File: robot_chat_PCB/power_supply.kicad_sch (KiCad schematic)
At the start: 23 parts, among them U2 MP1475DJ-LF-P, U3 MIC5317-3.3xM5

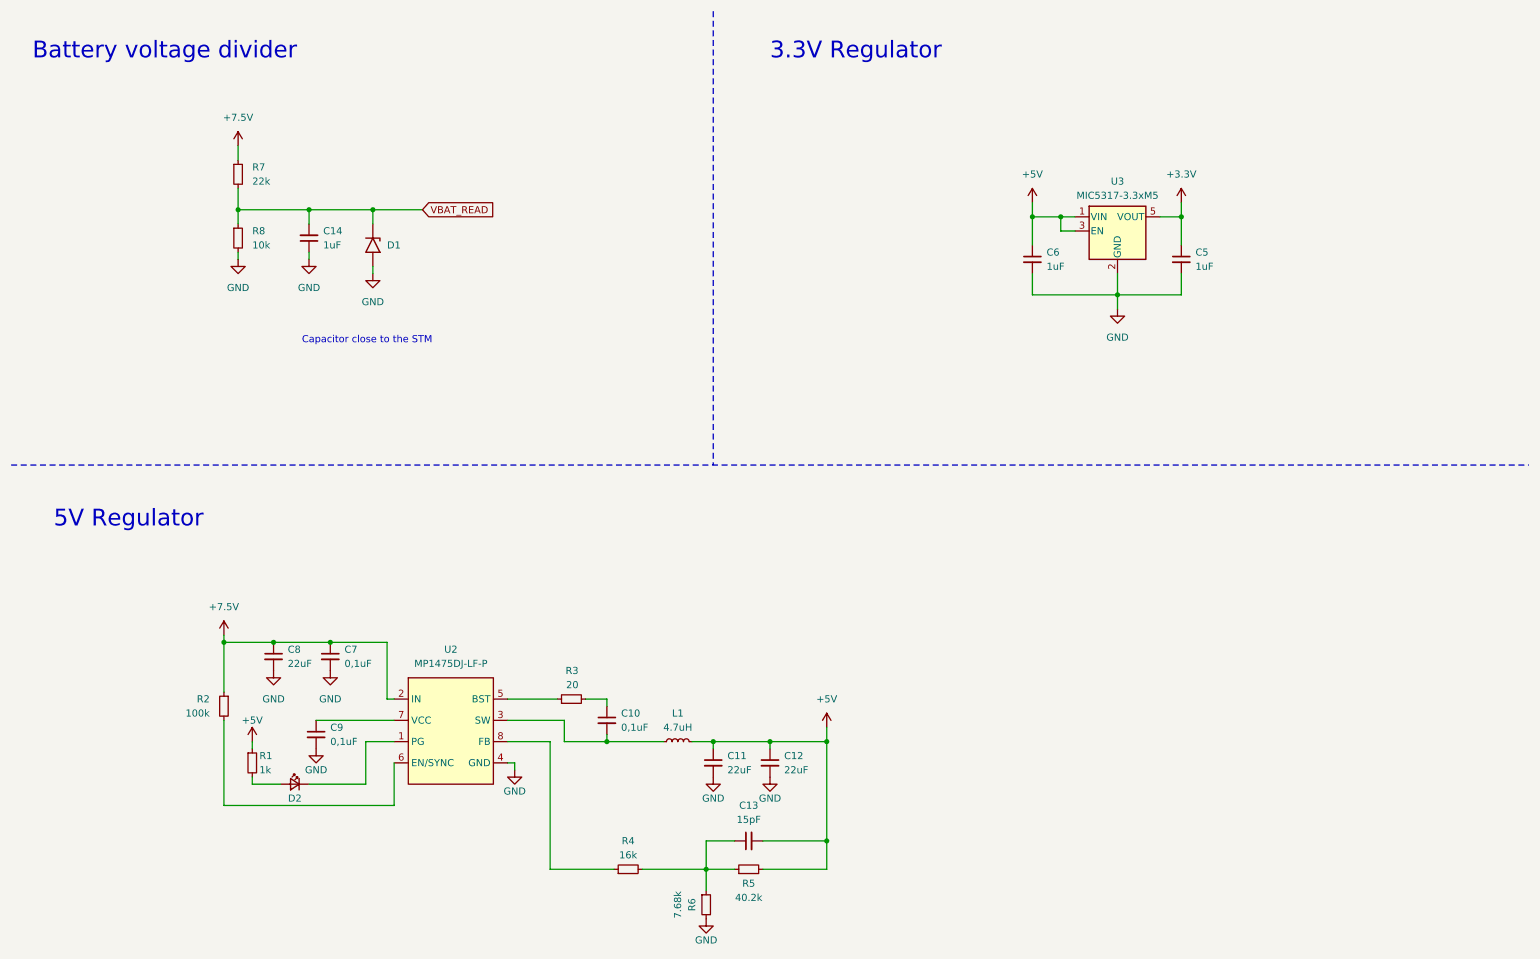
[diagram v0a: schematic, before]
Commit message: pcb alim et connecteurs
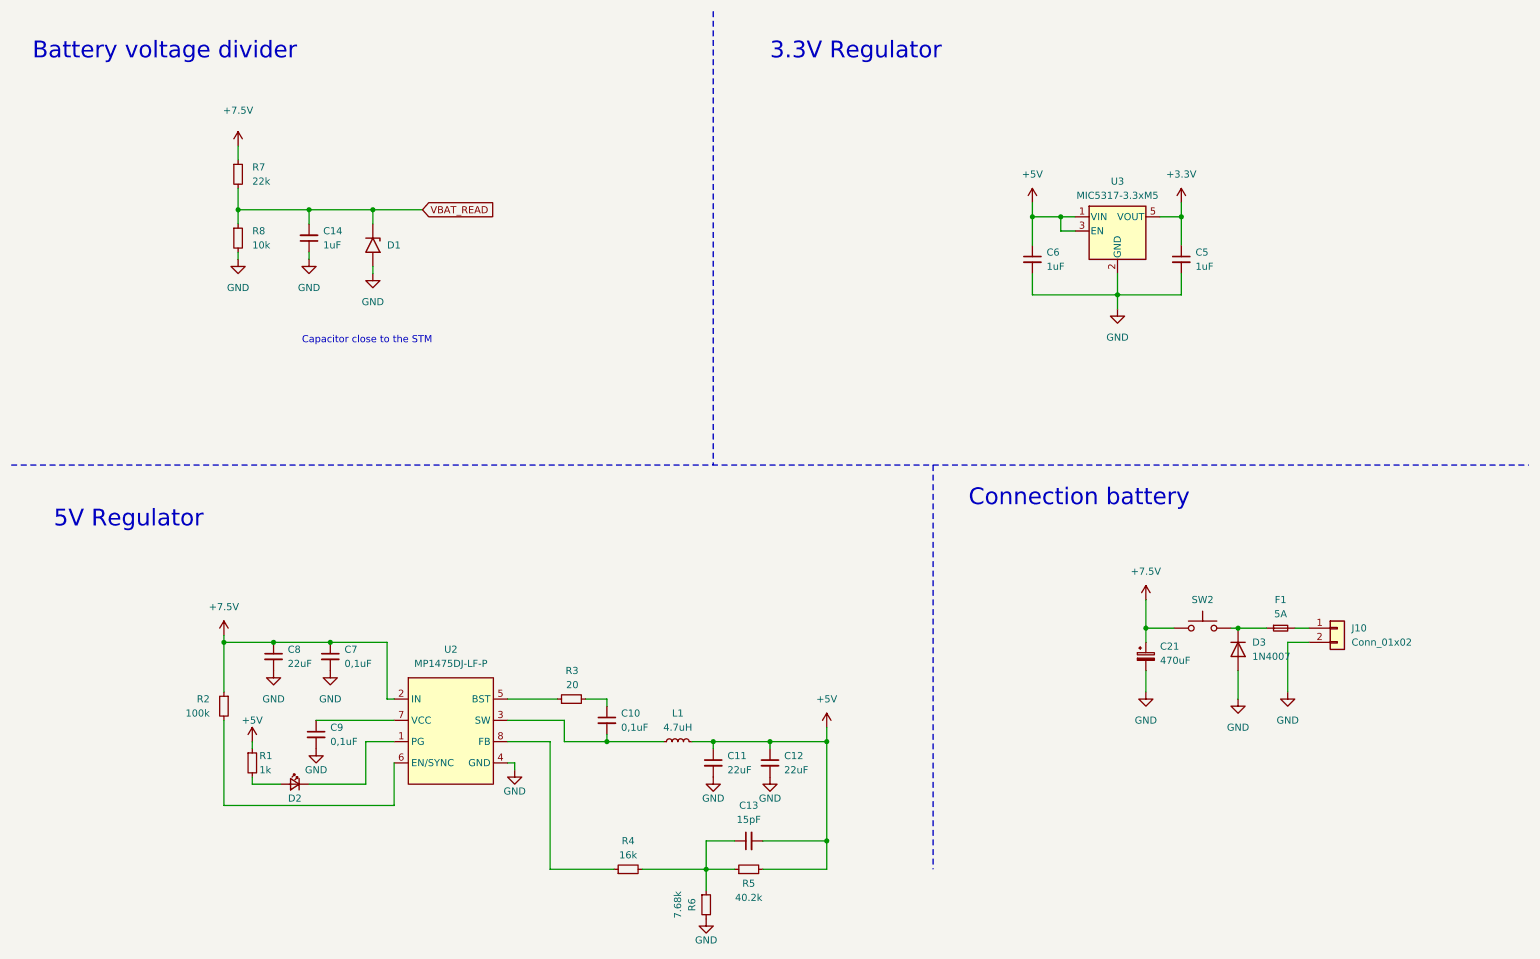
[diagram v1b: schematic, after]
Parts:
- added C21: 470uF, symbol Device:C_Polarized_Small
- added D3: 1N4007, Diode_THT:D_DO-41_SOD81_P10.16mm_Horizontal, symbol Diode:1N4007
- added F1: 5A, symbol Device:Fuse_Small
- added J10: Conn_01x02, symbol Connector_Generic:Conn_01x02
- added SW2: SW_Push, symbol Switch:SW_Push
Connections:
- net +7.5V: now also C21.1, SW2.1
- net GND: now also C21.2, D3.2 (A), J10.2 (Pin_2)
- new net: D3.1 (K), F1.1, SW2.2
- new net: F1.2, J10.1 (Pin_1)
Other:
- note added: "Connection battery"
